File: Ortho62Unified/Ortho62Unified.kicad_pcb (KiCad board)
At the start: 2 copper layers, 156 parts, among them J1 USB_B_Micro, SW1 SW_Push, SW10 SW_Push, SW11 SW_Push, SW12 SW_Push, SW13 SW_Push, SW14 SW_Push, SW15 SW_Push, SW16 SW_Push, SW17 SW_Push, SW18 SW_Push, SW19 SW_Push, SW2 SW_Push, SW20 SW_Push, SW21 SW_Push, SW22 SW_Push, SW23 SW_Push, SW24 SW_Push, SW25 SW_Push, SW26 SW_Push, SW27 SW_Push, SW28 SW_Push, SW29 SW_Push, SW3 SW_Push, SW30 SW_Push, SW31 SW_Push, SW32 SW_Push, SW33 SW_Push, SW34 SW_Push, SW35 SW_Push, SW36 SW_Push, SW37 SW_Push, SW38 SW_Push, SW39 SW_Push, SW4 SW_Push, SW40 SW_Push, SW41 SW_Push, SW42 SW_Push, SW43 SW_Push, SW44 SW_Push, SW45 SW_Push, SW46 SW_Push, SW47 SW_Push, SW48 SW_Push, SW49 SW_Push, SW5 SW_Push, SW50 SW_Push, SW51 SW_Push, SW52 SW_Push, SW53 SW_Push, SW54 SW_Push, SW55 SW_Push, SW56 SW_Push, SW57 SW_Push, SW58 SW_Push, SW59 SW_Push, SW6 SW_Push, SW60 SW_Push, SW61 SW_Push, SW62 SW_Push, SW63 SW_Push, SW64 SW_Push, SW65 SW_Push, SW66 SW_Push, SW7 SW_Push, SW8 SW_Push, SW9 SW_Push, U1 MCP1700T-3302E_TT, U2 RP2040

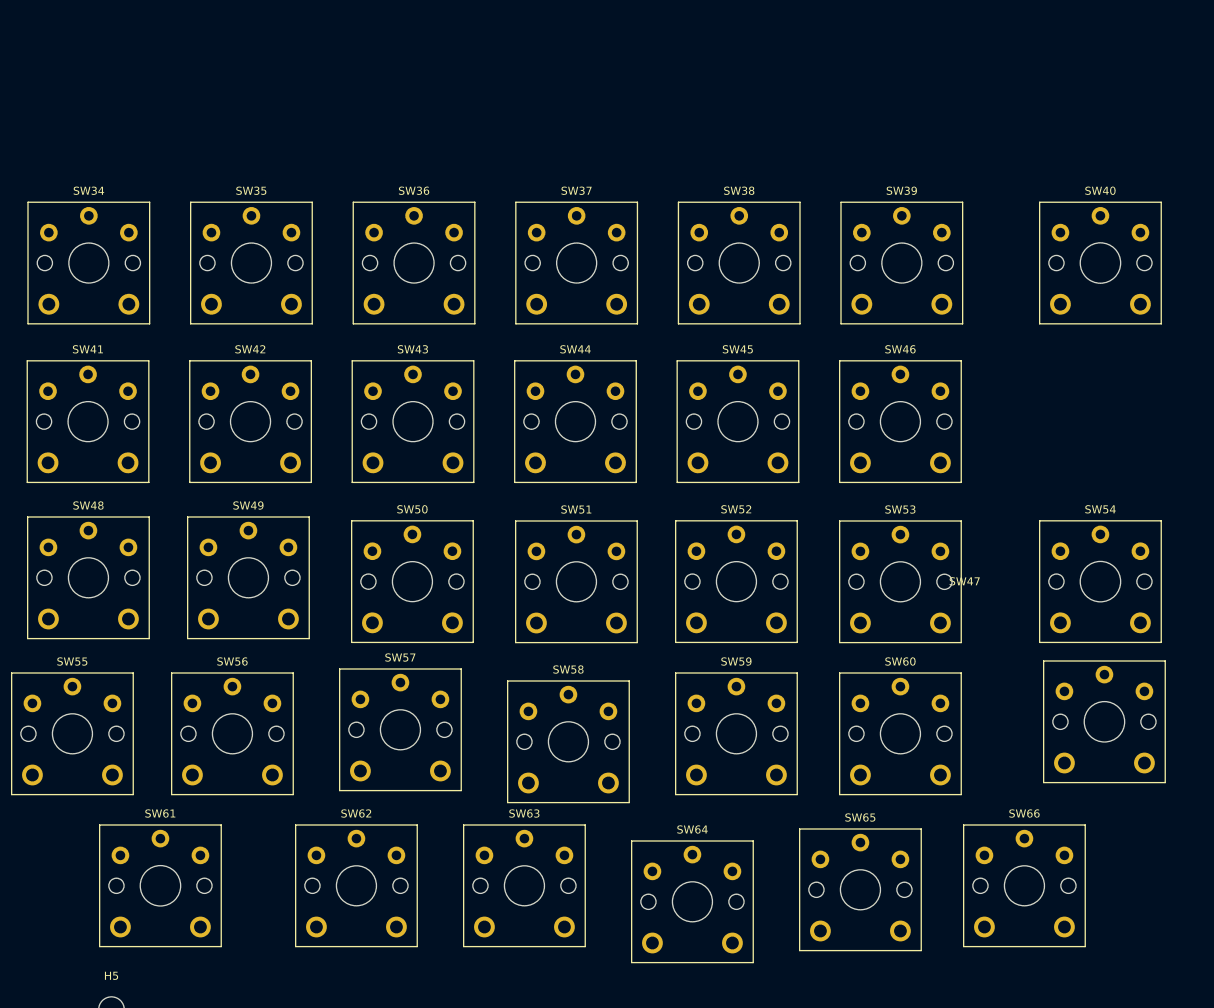
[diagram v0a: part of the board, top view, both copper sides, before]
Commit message: Rearrange keys, add AVR micro.
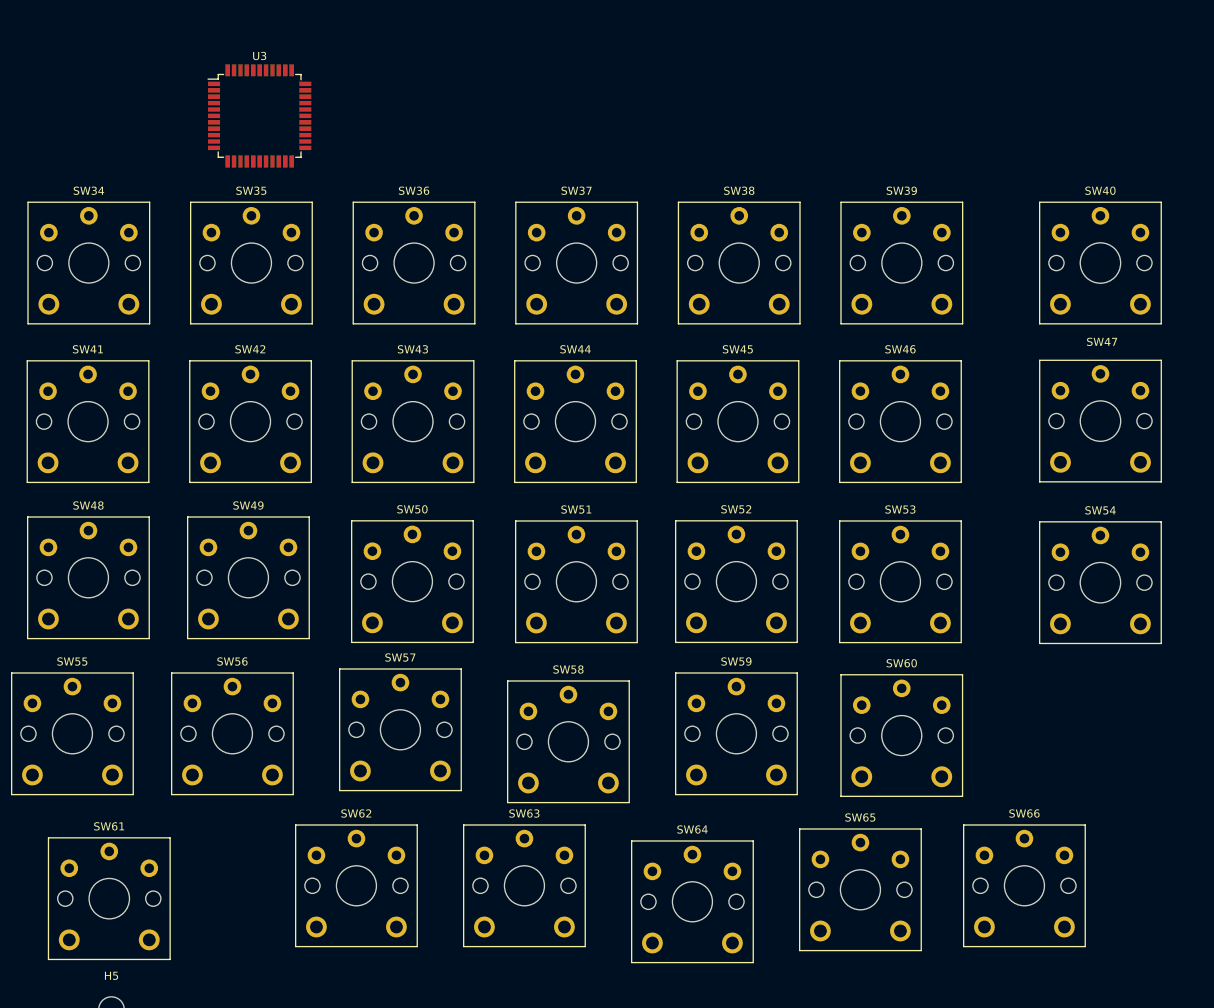
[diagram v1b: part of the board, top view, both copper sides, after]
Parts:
- added U3: ATxmega32A4U-A, Package_QFP:TQFP-44_10x10mm_P0.8mm, F.Cu at (215.9, 48.3)
- moved SW47 37.6 mm to (321.0, 86.4)
- moved SW61 6.60 mm to (197.1, 146.1)
- moved SW60 0.27 mm to (296.2, 125.7)
- moved SW54 0.13 mm to (321.0, 106.6)

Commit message: 66 symmetrical layout.
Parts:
- SW66: footprint Switch_Keyboard_Kailh:SW_Kailh_Choc_V1V2_1.00u -> Switch_Keyboard_Kailh:SW_Kailh_Choc_V1V2_1.50u
- moved SW66 21.0 mm to (321.0, 125.7)
- moved SW61 10.2 mm to (207.3, 145.6)
- moved SW30 9.54 mm to (157.0, 145.6)
- moved SW27 7.99 mm to (91.5, 145.5)
- moved SW26 7.86 mm to (71.5, 145.5)
- moved SW28 7.50 mm to (111.8, 145.6)
- moved SW29 7.18 mm to (132.1, 145.6)
- moved SW63 5.64 mm to (254.4, 146.0)
- moved SW64 5.41 mm to (275.3, 145.6)
- moved SW65 5.18 mm to (296.2, 144.6)
- moved SW62 4.84 mm to (232.7, 145.8)
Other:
- board text added: "MacSplit66 Keyboard by Neeraj Adsul Copyright 2022, 125 Systems. Revision 1"
- board text removed: "MacSplit60 Keyboard by Neeraj Adsul Copyright 2022, 125 Systems. Revision 1"

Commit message: Add cutout border for 3D visualisation
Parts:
- moved C1 149.3 mm to (319.8, 174.3)
- moved C10 149.3 mm to (316.1, 183.6)
- moved C11 149.3 mm to (304.1, 184.3)
- moved C13 149.3 mm to (319.8, 176.8)
- moved C2 149.3 mm to (312.1, 183.6)
- moved C3 149.3 mm to (323.8, 171.8)
- moved C4 149.3 mm to (312.8, 181.1)
- moved C5 149.3 mm to (300.1, 184.3)
- moved C6 149.3 mm to (304.8, 181.1)
- moved C7 149.3 mm to (323.8, 176.8)
- moved C8 149.3 mm to (319.8, 171.8)
- moved C9 149.3 mm to (308.8, 181.1)
- moved J1 149.3 mm to (303.3, 173.7)
- moved R1 149.3 mm to (323.8, 174.3)
- moved R2 149.3 mm to (316.8, 181.1)
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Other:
- board outline added: 317.5 x 149.9 mm

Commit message: Align and correctly space 66 keys.
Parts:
- removed C1, C2: 1u, Capacitor_SMD:C_0603_1608Metric
- removed R1, R2: 27.4, Resistor_SMD:R_0603_1608Metric
- added F1: Polyfuse, Fuse:Fuse_1206_3216Metric_Pad1.42x1.75mm_HandSolder, F.Cu at (292.3, 194.4)
- added FB1: FerriteBead, Fuse:Fuse_0603_1608Metric_Pad1.05x0.95mm_HandSolder, F.Cu at (300.6, 188.9)
- U2: value RP2040 -> USBLC6-2SC6; footprint Package_DFN_QFN:QFN-56-1EP_7x7mm_P0.4mm_EP3.2x3.2mm -> Package_TO_SOT_SMD:SOT-23-6
- moved H7 192.0 mm to (277.6, 208.6)
- moved U3 144.5 mm to (202.5, 49.7)
- moved C7 24.8 mm to (329.2, 201.0)
- moved C10 24.8 mm to (321.5, 207.8)
- moved C13 24.8 mm to (325.2, 201.0)
- moved D19 24.8 mm to (143.5, 189.8)
- moved D20 24.8 mm to (162.7, 192.9)
- moved D22 24.8 mm to (84.1, 199.5)
- moved D23 24.8 mm to (103.8, 199.5)
- moved D28 24.8 mm to (76.6, 199.3)
- moved D36 24.8 mm to (240.9, 207.1)
- moved D37 24.8 mm to (205.5, 207.1)
- moved D38 24.8 mm to (225.7, 207.1)
- moved D42 24.8 mm to (220.7, 207.1)
- moved D43 24.8 mm to (245.9, 207.1)
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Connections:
- C10 pad 1: +3V3 -> unconnected-(C10-Pad1)
- C10 pad 2: Net-(C10-Pad2) -> unconnected-(C10-Pad2)
- C11 pad 1: +3V3 -> /VBUS
- C11 pad 2: Net-(C10-Pad2) -> GND
- C12 pad 1: Net-(J1-VBUS) -> /VBUS_FUSED
- C3 pad 1: +1V1 -> unconnected-(C3-Pad1)
- C3 pad 2: GND -> unconnected-(C3-Pad2)
- C4 pad 1: +1V1 -> unconnected-(C4-Pad1)
- C4 pad 2: GND -> unconnected-(C4-Pad2)
- C5 pad 2: Net-(C10-Pad2) -> GND
- C6 pad 1: +3V3 -> Net-(U3-AVCC)
- C6 pad 2: Net-(C10-Pad2) -> GND
- C7 pad 1: +3V3 -> unconnected-(C7-Pad1)
- C7 pad 2: Net-(C10-Pad2) -> unconnected-(C7-Pad2)
- C8 pad 1: +3V3 -> unconnected-(C8-Pad1)
- C8 pad 2: Net-(C10-Pad2) -> unconnected-(C8-Pad2)
- C9 pad 1: +3V3 -> unconnected-(C9-Pad1)
- C9 pad 2: Net-(C10-Pad2) -> unconnected-(C9-Pad2)
- J1 pad 1: Net-(J1-VBUS) -> /VBUS
- U1 pad 3: Net-(J1-VBUS) -> /VBUS_FUSED
- U2 pad 1: +3V3 -> /USB_D-
- U2 pad 2: unconnected-(U2-GPIO0-Pad2) -> GND
- U2 pad 3: unconnected-(U2-GPIO1-Pad3) -> /USB_D+
- U2 pad 4: unconnected-(U2-GPIO2-Pad4) -> /USBM+
- U2 pad 5: unconnected-(U2-GPIO3-Pad5) -> /VBUS
- U2 pad 6: unconnected-(U2-GPIO4-Pad6) -> /USBM-
- U3 pad 19: Net-(U3-VCC-Pad19) -> +3V3
- U3 pad 26: unconnected-(U3-PD6-Pad26) -> /USBM-
- U3 pad 27: unconnected-(U3-PD7-Pad27) -> /USBM+
- U3 pad 31: Net-(U3-VCC-Pad19) -> +3V3
- U3 pad 34: unconnected-(U3-PDI_DATA-Pad34) -> Net-(J4-DATA)
- U3 pad 35: unconnected-(U3-~{RESET}/PDI_CLK-Pad35) -> Net-(J4-CLOCK)
- U3 pad 39: unconnected-(U3-AVCC-Pad39) -> Net-(U3-AVCC)
- U3 pad 9: Net-(U3-VCC-Pad19) -> +3V3
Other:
- board size 317.5 x 149.9 mm -> 300 x 135 mm

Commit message: Add function keys row.
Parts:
- removed C10, C7, C8, C9: 100n, Capacitor_SMD:C_0603_1608Metric
- removed the C3 at (329.2, 196.0)
- removed the C4 at (318.2, 205.3)
- added D55: 1N4148W, Diode_SMD:D_SOD-123, F.Cu at (318.6, 186.7)
- added D68: 1N4148W, Diode_SMD:D_SOD-123, F.Cu at (318.6, 189.6)
- added D69: 1N4148W, Diode_SMD:D_SOD-123, F.Cu at (-65.0, 105.5)
- added D70: 1N4148W, Diode_SMD:D_SOD-123, F.Cu at (-65.0, 108.8)
- added D71: 1N4148W, Diode_SMD:D_SOD-123, F.Cu at (-65.0, 112.2)
- added D72: 1N4148W, Diode_SMD:D_SOD-123, F.Cu at (-65.0, 115.5)
- added D73: 1N4148W, Diode_SMD:D_SOD-123, F.Cu at (-65.0, 118.9)
- added D74: 1N4148W, Diode_SMD:D_SOD-123, F.Cu at (-59.2, 105.5)
- added D75: 1N4148W, Diode_SMD:D_SOD-123, F.Cu at (-59.2, 108.8)
- added D76: 1N4148W, Diode_SMD:D_SOD-123, F.Cu at (-59.2, 112.2)
- added D77: 1N4148W, Diode_SMD:D_SOD-123, F.Cu at (-59.2, 115.5)
- added D78: 1N4148W, Diode_SMD:D_SOD-123, F.Cu at (-59.2, 118.9)
- added D79: 1N4148W, Diode_SMD:D_SOD-123, F.Cu at (-53.4, 105.5)
- added D80: 1N4148W, Diode_SMD:D_SOD-123, F.Cu at (-53.4, 108.8)
- added D81: 1N4148W, Diode_SMD:D_SOD-123, F.Cu at (-53.4, 112.2)
- added D82: 1N4148W, Diode_SMD:D_SOD-123, F.Cu at (-53.4, 115.5)
- added J3: USB_C_Receptacle_USB2.0, CustomHandSolderConnectors:USB_C_Receptacle_GCT_USB4085_HandSolder_SMT, F.Cu at (188.7, 236.0)
- added SW55: SW_Push, Switch_Keyboard_Kailh:SW_Kailh_Choc_V1V2_1.00u, F.Cu at (309.0, 161.0)
- added SW68: SW_Push, Switch_Keyboard_Kailh:SW_Kailh_Choc_V1V2_1.00u, F.Cu at (329.0, 161.1)
- added SW69: SW_Push, Switch_Keyboard_Kailh:SW_Kailh_Choc_V1V2_1.00u, F.Cu at (79.8, 65.0)
- added SW70: SW_Push, Switch_Keyboard_Kailh:SW_Kailh_Choc_V1V2_1.00u, F.Cu at (100.2, 63.7)
- added SW71: SW_Push, Switch_Keyboard_Kailh:SW_Kailh_Choc_V1V2_1.00u, F.Cu at (120.2, 63.4)
- added SW72: SW_Push, Switch_Keyboard_Kailh:SW_Kailh_Choc_V1V2_1.00u, F.Cu at (139.8, 64.3)
- added SW73: SW_Push, Switch_Keyboard_Kailh:SW_Kailh_Choc_V1V2_1.00u, F.Cu at (160.0, 64.1)
- added SW74: SW_Push, Switch_Keyboard_Kailh:SW_Kailh_Choc_V1V2_1.00u, F.Cu at (180.6, 64.7)
- added SW75: SW_Push, Switch_Keyboard_Kailh:SW_Kailh_Choc_V1V2_1.50u, F.Cu at (55.2, 64.7)
- added SW76: SW_Push, Switch_Keyboard_Kailh:SW_Kailh_Choc_V1V2_1.00u, F.Cu at (200.0, 64.8)
- added SW77: SW_Push, Switch_Keyboard_Kailh:SW_Kailh_Choc_V1V2_1.00u, F.Cu at (220.4, 64.8)
- added SW78: SW_Push, Switch_Keyboard_Kailh:SW_Kailh_Choc_V1V2_1.00u, F.Cu at (240.2, 64.9)
- added SW79: SW_Push, Switch_Keyboard_Kailh:SW_Kailh_Choc_V1V2_1.00u, F.Cu at (260.0, 65.0)
- added SW80: SW_Push, Switch_Keyboard_Kailh:SW_Kailh_Choc_V1V2_1.00u, F.Cu at (280.2, 65.1)
- added SW81: SW_Push, Switch_Keyboard_Kailh:SW_Kailh_Choc_V1V2_1.00u, F.Cu at (301.0, 64.6)
- added SW82: SW_Push, Switch_Keyboard_Kailh:SW_Kailh_Choc_V1V2_1.50u, F.Cu at (325.6, 64.6)
- C1: renamed from C5; value 100n -> C; footprint Capacitor_SMD:C_0603_1608Metric -> Capacitor_SMD:C_0603_1608Metric_Pad1.08x0.95mm_HandSolder
- C2: renamed from C6; value 100n -> C; footprint Capacitor_SMD:C_0603_1608Metric -> Capacitor_SMD:C_0603_1608Metric_Pad1.08x0.95mm_HandSolder
- C3: renamed from C12; value 1u -> C; footprint Capacitor_SMD:C_0603_1608Metric -> Capacitor_SMD:C_0603_1608Metric_Pad1.08x0.95mm_HandSolder
- C4: renamed from C13; value 1u -> C; footprint Capacitor_SMD:C_0603_1608Metric -> Capacitor_SMD:C_0603_1608Metric_Pad1.08x0.95mm_HandSolder
- C5: renamed from C11; value 100n -> C; footprint Capacitor_SMD:C_0603_1608Metric -> Capacitor_SMD:C_0603_1608Metric_Pad1.08x0.95mm_HandSolder
- D1, D2, D3, D4, D5, D6, D7: footprint Diode_SMD:D_SOD-323_Hand_Split_Keyboard -> Diode_SMD:D_SOD-123
- D10: renamed from D36; footprint Diode_SMD:D_SOD-323_Hand_Split_Keyboard -> Diode_SMD:D_SOD-123
- D11: renamed from D37; footprint Diode_SMD:D_SOD-323_Hand_Split_Keyboard -> Diode_SMD:D_SOD-123
- D12: renamed from D38; footprint Diode_SMD:D_SOD-323_Hand_Split_Keyboard -> Diode_SMD:D_SOD-123
- D13: renamed from D39; footprint Diode_SMD:D_SOD-323_Hand_Split_Keyboard -> Diode_SMD:D_SOD-123
- D14: renamed from D40; footprint Diode_SMD:D_SOD-323_Hand_Split_Keyboard -> Diode_SMD:D_SOD-123
- D15: renamed from D10; footprint Diode_SMD:D_SOD-323_Hand_Split_Keyboard -> Diode_SMD:D_SOD-123
- D16: renamed from D11; footprint Diode_SMD:D_SOD-323_Hand_Split_Keyboard -> Diode_SMD:D_SOD-123
- D17: renamed from D12; footprint Diode_SMD:D_SOD-323_Hand_Split_Keyboard -> Diode_SMD:D_SOD-123
- D18: renamed from D13; footprint Diode_SMD:D_SOD-323_Hand_Split_Keyboard -> Diode_SMD:D_SOD-123
- D19: renamed from D14; footprint Diode_SMD:D_SOD-323_Hand_Split_Keyboard -> Diode_SMD:D_SOD-123
- D20: renamed from D15; footprint Diode_SMD:D_SOD-323_Hand_Split_Keyboard -> Diode_SMD:D_SOD-123
- D21: renamed from D8; footprint Diode_SMD:D_SOD-323_Hand_Split_Keyboard -> Diode_SMD:D_SOD-123
- D22: renamed from D41; footprint Diode_SMD:D_SOD-323_Hand_Split_Keyboard -> Diode_SMD:D_SOD-123
- D23: renamed from D42; footprint Diode_SMD:D_SOD-323_Hand_Split_Keyboard -> Diode_SMD:D_SOD-123
- D24: renamed from D43; footprint Diode_SMD:D_SOD-323_Hand_Split_Keyboard -> Diode_SMD:D_SOD-123
- D25: renamed from D44; footprint Diode_SMD:D_SOD-323_Hand_Split_Keyboard -> Diode_SMD:D_SOD-123
- D26: renamed from D45; footprint Diode_SMD:D_SOD-323_Hand_Split_Keyboard -> Diode_SMD:D_SOD-123
- D27: renamed from D46; footprint Diode_SMD:D_SOD-323_Hand_Split_Keyboard -> Diode_SMD:D_SOD-123
- D28: renamed from D47; footprint Diode_SMD:D_SOD-323_Hand_Split_Keyboard -> Diode_SMD:D_SOD-123
- D29: renamed from D16; footprint Diode_SMD:D_SOD-323_Hand_Split_Keyboard -> Diode_SMD:D_SOD-123
- D30: renamed from D17; footprint Diode_SMD:D_SOD-323_Hand_Split_Keyboard -> Diode_SMD:D_SOD-123
- D31: renamed from D18; footprint Diode_SMD:D_SOD-323_Hand_Split_Keyboard -> Diode_SMD:D_SOD-123
- D32: renamed from D19; footprint Diode_SMD:D_SOD-323_Hand_Split_Keyboard -> Diode_SMD:D_SOD-123
- D33: renamed from D20; footprint Diode_SMD:D_SOD-323_Hand_Split_Keyboard -> Diode_SMD:D_SOD-123
- D34: renamed from D21; footprint Diode_SMD:D_SOD-323_Hand_Split_Keyboard -> Diode_SMD:D_SOD-123
- D35: renamed from D9; footprint Diode_SMD:D_SOD-323_Hand_Split_Keyboard -> Diode_SMD:D_SOD-123
- D36: renamed from D48; footprint Diode_SMD:D_SOD-323_Hand_Split_Keyboard -> Diode_SMD:D_SOD-123
- D37: renamed from D49; footprint Diode_SMD:D_SOD-323_Hand_Split_Keyboard -> Diode_SMD:D_SOD-123
- D38: renamed from D50; footprint Diode_SMD:D_SOD-323_Hand_Split_Keyboard -> Diode_SMD:D_SOD-123
- D39: renamed from D51; footprint Diode_SMD:D_SOD-323_Hand_Split_Keyboard -> Diode_SMD:D_SOD-123
- D40: renamed from D52; footprint Diode_SMD:D_SOD-323_Hand_Split_Keyboard -> Diode_SMD:D_SOD-123
- D41: renamed from D53; footprint Diode_SMD:D_SOD-323_Hand_Split_Keyboard -> Diode_SMD:D_SOD-123
- D42: renamed from D54; footprint Diode_SMD:D_SOD-323_Hand_Split_Keyboard -> Diode_SMD:D_SOD-123
- D43: renamed from D22; footprint Diode_SMD:D_SOD-323_Hand_Split_Keyboard -> Diode_SMD:D_SOD-123
- D44: renamed from D23; footprint Diode_SMD:D_SOD-323_Hand_Split_Keyboard -> Diode_SMD:D_SOD-123
- D45: renamed from D24; footprint Diode_SMD:D_SOD-323_Hand_Split_Keyboard -> Diode_SMD:D_SOD-123
- D46: renamed from D25; footprint Diode_SMD:D_SOD-323_Hand_Split_Keyboard -> Diode_SMD:D_SOD-123
- D47: renamed from D26; footprint Diode_SMD:D_SOD-323_Hand_Split_Keyboard -> Diode_SMD:D_SOD-123
- D48: renamed from D27; footprint Diode_SMD:D_SOD-323_Hand_Split_Keyboard -> Diode_SMD:D_SOD-123
- D49: renamed from D55; footprint Diode_SMD:D_SOD-323_Hand_Split_Keyboard -> Diode_SMD:D_SOD-123
- D50: renamed from D56; footprint Diode_SMD:D_SOD-323_Hand_Split_Keyboard -> Diode_SMD:D_SOD-123
- D51: renamed from D57; footprint Diode_SMD:D_SOD-323_Hand_Split_Keyboard -> Diode_SMD:D_SOD-123
- D52: renamed from D58; footprint Diode_SMD:D_SOD-323_Hand_Split_Keyboard -> Diode_SMD:D_SOD-123
- D53: renamed from D59; footprint Diode_SMD:D_SOD-323_Hand_Split_Keyboard -> Diode_SMD:D_SOD-123
- D54: renamed from D60; footprint Diode_SMD:D_SOD-323_Hand_Split_Keyboard -> Diode_SMD:D_SOD-123
- D56: renamed from D28; footprint Diode_SMD:D_SOD-323_Hand_Split_Keyboard -> Diode_SMD:D_SOD-123
- D57: renamed from D29; footprint Diode_SMD:D_SOD-323_Hand_Split_Keyboard -> Diode_SMD:D_SOD-123
- D58: renamed from D30; footprint Diode_SMD:D_SOD-323_Hand_Split_Keyboard -> Diode_SMD:D_SOD-123
- D59: renamed from D31; footprint Diode_SMD:D_SOD-323_Hand_Split_Keyboard -> Diode_SMD:D_SOD-123
- D60: renamed from D32; footprint Diode_SMD:D_SOD-323_Hand_Split_Keyboard -> Diode_SMD:D_SOD-123
- D61: renamed from D33; footprint Diode_SMD:D_SOD-323_Hand_Split_Keyboard -> Diode_SMD:D_SOD-123
- D62: renamed from D61; footprint Diode_SMD:D_SOD-323_Hand_Split_Keyboard -> Diode_SMD:D_SOD-123
- D63: renamed from D62; footprint Diode_SMD:D_SOD-323_Hand_Split_Keyboard -> Diode_SMD:D_SOD-123
- D64: renamed from D63; footprint Diode_SMD:D_SOD-323_Hand_Split_Keyboard -> Diode_SMD:D_SOD-123
- D65: renamed from D64; footprint Diode_SMD:D_SOD-323_Hand_Split_Keyboard -> Diode_SMD:D_SOD-123
- D66: renamed from D65; footprint Diode_SMD:D_SOD-323_Hand_Split_Keyboard -> Diode_SMD:D_SOD-123
- D67: renamed from D66; footprint Diode_SMD:D_SOD-323_Hand_Split_Keyboard -> Diode_SMD:D_SOD-123
- D8: renamed from D34; footprint Diode_SMD:D_SOD-323_Hand_Split_Keyboard -> Diode_SMD:D_SOD-123
- D9: renamed from D35; footprint Diode_SMD:D_SOD-323_Hand_Split_Keyboard -> Diode_SMD:D_SOD-123
- FB1: footprint Fuse:Fuse_0603_1608Metric_Pad1.05x0.95mm_HandSolder -> Inductor_SMD:L_0603_1608Metric_Pad1.05x0.95mm_HandSolder
- J1: value USB_B_Micro -> AVR-PDI-6; footprint Connector_USB:USB_Micro-B_Molex_47346-0001 -> Connector_PinHeader_2.54mm:PinHeader_2x03_P2.54mm_Horizontal
- SW57: renamed from SW26; footprint Switch_Keyboard_Kailh:SW_Kailh_Choc_V1V2_1.00u -> Switch_Keyboard_Kailh:SW_Kailh_Choc_V1V2_1.50u
- SW58: renamed from SW27; footprint Switch_Keyboard_Kailh:SW_Kailh_Choc_V1V2_1.00u -> Switch_Keyboard_Kailh:SW_Kailh_Choc_V1V2_1.50u
- moved J1 124.9 mm to (187.2, 227.1), turned to 0 degrees
- moved U2 83.3 mm to (119.4, 44.0)
- moved D21 28.7 mm to (37.2, 32.1)
- moved D7 28.7 mm to (33.2, 33.8)
- moved H5 25.9 mm to (29.0, 38.8)
- moved H3 24.5 mm to (140.0, 43.1)
- moved SW57 24.5 mm to (55.4, 161.0)
- moved SW58 15.5 mm to (84.4, 161.0)
- moved SW62 11.0 mm to (204.4, 160.9)
- moved SW61 11.0 mm to (175.4, 161.0)
- moved SW63 10.9 mm to (229.0, 160.8)
- moved SW64 10.9 mm to (249.0, 160.8)
- moved SW65 10.9 mm to (269.0, 161.0)
- moved SW66 10.9 mm to (289.0, 161.0)
- moved SW59 10.7 mm to (130.6, 161.0)
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- renumbered H2 to H1, H3 to H2, H4 to H3, H5 to H4, H6 to H5, H7 to H6, SW36 to SW10, SW37 to SW11, SW38 to SW12, SW39 to SW13, SW40 to SW14, SW7 to SW15, SW8 to SW16, SW9 to SW17, SW10 to SW18, SW11 to SW19, SW12 to SW20, SW32 to SW21, SW41 to SW22, SW42 to SW23, SW43 to SW24, SW44 to SW25, SW45 to SW26, SW46 to SW27, SW47 to SW28, SW13 to SW29, SW14 to SW30, SW15 to SW31, SW16 to SW32, SW17 to SW33, SW18 to SW34, SW33 to SW35, SW48 to SW36, SW49 to SW37, SW50 to SW38, SW51 to SW39, SW52 to SW40, SW53 to SW41, SW54 to SW42, SW19 to SW43, SW20 to SW44, SW21 to SW45, SW22 to SW46, SW23 to SW47, SW24 to SW48, SW55 to SW49, SW56 to SW50, SW57 to SW51, SW58 to SW52, SW59 to SW53, SW60 to SW54, SW25 to SW56, SW28 to SW59, SW29 to SW60, SW30 to SW61, SW61 to SW62, SW62 to SW63, SW63 to SW64, SW64 to SW65, SW65 to SW66, SW66 to SW67, SW31 to SW7, SW34 to SW8, SW35 to SW9, U3 to U2, U2 to U3
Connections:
- J1 pad 1: /VBUS -> Net-(J1-DATA)
- J1 pad 2: /USB_D- -> +3V3
- J1 pad 3: /USB_D+ -> unconnected-(J1-NC-Pad3)
- J1 pad 5: GND -> Net-(J1-CLOCK)
- J1 pad 6: unconnected-(J1-Shield-Pad6) -> GND
- U2 pad 18: Net-(U3-GND-Pad18) -> GND
- U2 pad 30: Net-(U3-GND-Pad18) -> GND
- U2 pad 34: Net-(J4-DATA) -> Net-(J1-DATA)
- U2 pad 35: Net-(J4-CLOCK) -> Net-(J1-CLOCK)
- U2 pad 38: Net-(U3-GND-Pad18) -> GND
- U2 pad 8: Net-(U3-GND-Pad18) -> GND
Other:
- board size 300 x 135 mm -> 300 x 140 mm

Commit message: Place and align all 82 keys.
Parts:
- SW57, SW58: footprint Switch_Keyboard_Kailh:SW_Kailh_Choc_V1V2_1.50u -> Switch_Keyboard_Kailh:SW_Kailh_Choc_V1V2_1.00u
- moved SW57 4.74 mm to (59.9, 162.5)
- moved SW58 4.74 mm to (79.9, 162.5)
- moved SW71 1.63 mm to (119.9, 65.0)
- moved SW55 1.50 mm to (309.0, 162.5)
- moved SW59 1.50 mm to (130.6, 162.5)
- moved SW60 1.50 mm to (150.6, 162.5)
- moved SW61 1.50 mm to (175.4, 162.5)
- moved SW62 1.50 mm to (204.4, 162.4)
- moved SW63 1.50 mm to (229.0, 162.3)
- moved SW64 1.50 mm to (249.0, 162.3)
- moved SW65 1.50 mm to (269.0, 162.5)
- moved SW66 1.50 mm to (289.0, 162.5)
- moved SW68 1.50 mm to (329.0, 162.6)
- moved SW70 1.33 mm to (99.9, 65.0)
- moved SW82 1.26 mm to (324.4, 65.0)
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
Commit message: Place all diodes within keys.
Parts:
- D1, D15, D16, D17, D18, D19, D2, D20, D29, D3, D30, D31, D32, D33, D34, D4, D43, D44, D45, D46, D47, D48, D5, D56, D57, D58, D59, D6, D60, D61: moved to F.Cu
- moved D82 380.5 mm to (324.4, 69.8)
- moved D81 355.8 mm to (299.9, 69.8)
- moved D80 335.9 mm to (280.2, 69.8)
- moved D79 315.4 mm to (260.0, 69.8)
- moved H1 311.6 mm to (334.3, 49.1)
- moved D78 303.4 mm to (240.2, 69.8)
- moved D77 282.8 mm to (219.9, 69.8)
- moved D76 262.5 mm to (199.9, 69.8)
- moved D74 241.7 mm to (179.9, 69.8)
- moved D73 230.2 mm to (159.9, 69.8)
- moved C1 220.8 mm to (156.2, 45.8)
- moved C2 220.8 mm to (160.9, 42.6)
- moved C3 220.8 mm to (151.1, 28.8)
- moved C4 220.8 mm to (176.0, 38.3)
- moved C5 220.8 mm to (160.2, 45.8)
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
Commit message: Route rows and colums of keyboard matrix to 1.27mm headers.
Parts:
- added J2: Conn_01x06_Socket, Connector_PinHeader_1.27mm:PinHeader_1x06_P1.27mm_Vertical, F.Cu at (48.9, 53.7)
- added J4: Conn_01x08_Socket, Connector_PinHeader_1.27mm:PinHeader_1x08_P1.27mm_Vertical, F.Cu at (137.9, 52.0)
- added J5: Conn_01x06_Socket, Connector_PinHeader_1.27mm:PinHeader_1x06_P1.27mm_Vertical, F.Cu at (219.9, 53.4)
- D1, D10, D11, D12, D13, D14, D15, D16, D17, D18, D19, D2, D20, D21, D22, D23, D24, D25, D26, D27, D28, D29, D3, D30, D31, D32, D33, D34, D35, D36, D37, D38, D39, D4, D40, D41, D42, D43, D44, D45, D46, D47, D48, D49, D5, D50, D51, D52, D53, D54, D55, D56, D57, D58, D59, D6, D60, D61, D62, D63, D64, D65, D66, D67, D68, D69, D7, D70, D71, D72, D73, D74, D75, D76, D77, D78, D79, D8, D80, D81, D82, D9: moved to B.Cu
- moved J3 192.1 mm to (270.5, 42.4), turned to 180 degrees
- moved U2 129.7 mm to (249.1, 44.5)
- moved U3 115.0 mm to (264.2, 46.4), turned to 180 degrees
- moved H1 32.6 mm to (301.7, 47.6)
- moved FB1 5.85 mm to (153.4, 31.7)
- moved C3 4.75 mm to (147.4, 31.7)
- moved C1 0.82 mm to (156.3, 46.6)
- moved C5 0.82 mm to (160.2, 46.6)
- turned D1 to 0 degrees
- turned D15 to 0 degrees
- turned D16 to 0 degrees
- turned D17 to 0 degrees
- turned D18 to 0 degrees
- turned D19 to 0 degrees
- turned D2 to 0 degrees
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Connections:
- D76 pad 1: /ROW_0 -> /ROW_F
- D77 pad 1: /ROW_0 -> /ROW_F
- D78 pad 1: /ROW_0 -> /ROW_F
- D79 pad 1: /ROW_0 -> /ROW_F
- D80 pad 1: /ROW_0 -> /ROW_F
- D81 pad 1: /ROW_0 -> /ROW_F
- D82 pad 1: /ROW_0 -> /ROW_F
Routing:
- net /ROW_4: track 0.00 -> 447.5 mm
- net /ROW_3: track 0.00 -> 404.3 mm
- net /ROW_2: track 0.00 -> 394.1 mm
- net /ROW_1: track 0.00 -> 372.0 mm
- net /ROW_0: track 0.00 -> 342.8 mm
- net /ROW_F: track 0.00 -> 326.1 mm
- net /COL_13: track 0.00 -> 250.2 mm
- net /COL_11: track 0.00 -> 224.2 mm
- net /COL_12: track 0.00 -> 221.0 mm
- net /COL_7: track 0.00 -> 210.7 mm
- net /COL_1: track 0.00 -> 210.0 mm
- net /COL_0: track 0.00 -> 202.8 mm
- net /COL_10: track 0.00 -> 198.8 mm
- net /COL_2: track 0.00 -> 186.7 mm
- net /COL_5: track 0.00 -> 184.5 mm
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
